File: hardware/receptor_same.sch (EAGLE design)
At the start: 62 parts, among them J1 ICSP, J2 SERIAL, J3 GPIO, J4 AUX-POWER, Q1 MMBT3904LT1G, U1 ATMEGA328P_TQFP, U2 SI4707, U3 TPA6111A2DR, U4 MCP16301/H, U5 TLV70233DBVR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

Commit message: fix mpn conector 3 pines
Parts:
- J4: MPN (none) -> P125-1103A1BS116A1
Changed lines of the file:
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@@
 <part name="GND19" library="supply1" library_urn="urn:adsk.eagle:library:371" deviceset="GND" device=""/>
 <part name="R16" library="OPL_Resistor" library_urn="urn:adsk.eagle:library:8004883" deviceset="SMD-RES-1.5K-5%-1/10W(0603)" device="" package3d_urn="urn:adsk.eagle:package:8004941/1" value="1.5K"/>
-<part name="J4" library="OPL_Connector" library_urn="urn:adsk.eagle:library:8004395" deviceset="DIP-BLACK-MALE-HEADER-VERT(3P-2.54)" device="" package3d_urn="urn:adsk.eagle:package:8004514/1" value="AUX-POWER"/>
+<part name="J4" library="OPL_Connector" library_urn="urn:adsk.eagle:library:8004395" deviceset="DIP-BLACK-MALE-HEADER-VERT(3P-2.54)" device="" package3d_urn="urn:adsk.eagle:package:8004514/1" value="AUX-POWER">
+<attribute name="MPN" value="P125-1103A1BS116A1"/>
+</part>
 <part name="P+17" library="supply1" library_urn="urn:adsk.eagle:library:371" deviceset="+3V3" device=""/>
 <part name="GND20" library="supply1" library_urn="urn:adsk.eagle:library:371" deviceset="GND" device=""/>
@@
 <attribute name="VALUE" x="96.52" y="16.51" size="1.27" layer="96" ratio="10"/>
 <attribute name="NAME" x="96.52" y="30.48" size="1.27" layer="95" ratio="10"/>
+<attribute name="MPN" x="99.06" y="24.13" size="1.778" layer="96" display="off"/>
 </instance>
 <instance part="P+17" gate="G$1" x="88.9" y="34.29" smashed="yes">

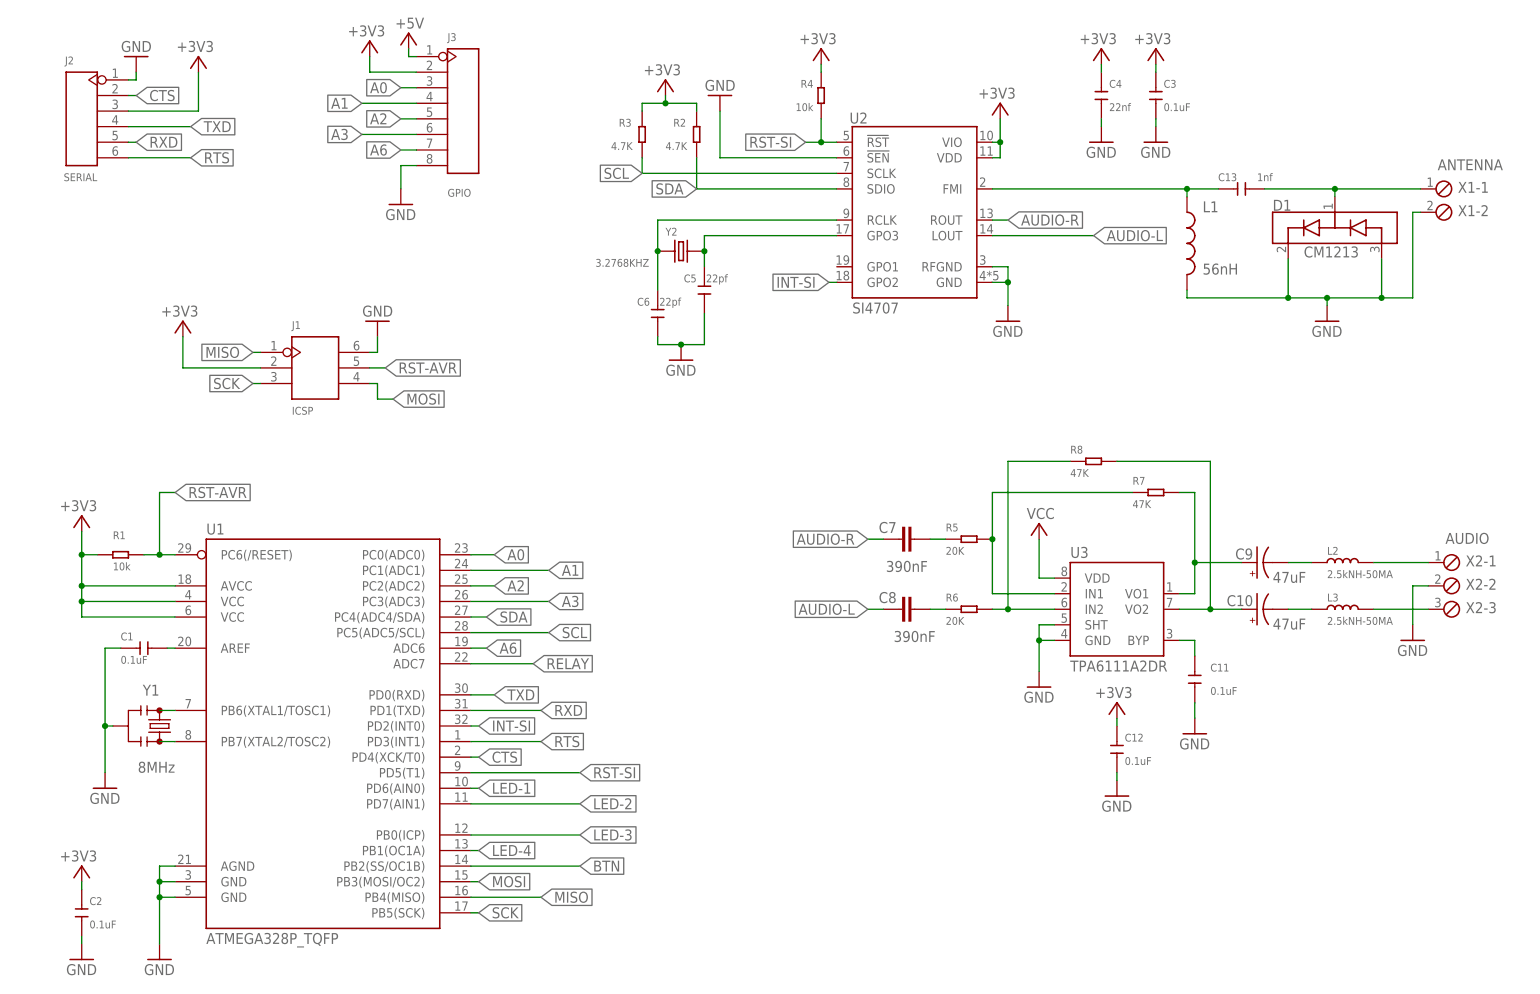
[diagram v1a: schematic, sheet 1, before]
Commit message: ajustes bom y posicion en hoja
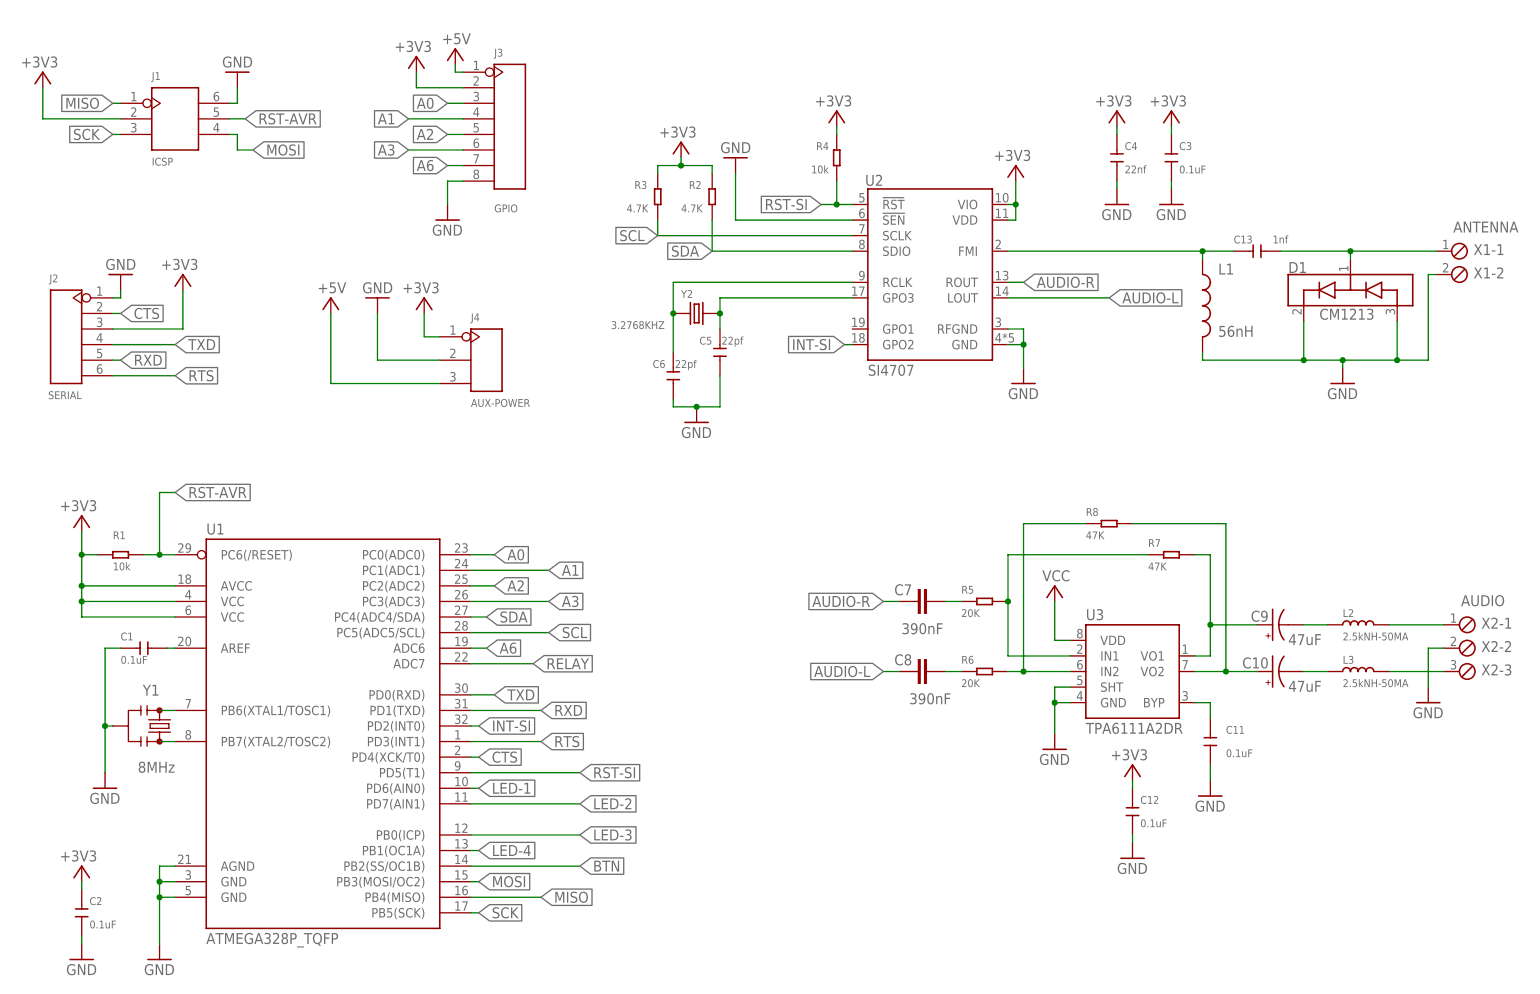
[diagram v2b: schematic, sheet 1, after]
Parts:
- C11, C12, C3: SPICEPREFIX C -> (none)
- D2: value LED-1 -> GREEN
- D3: value LED-2 -> GREEN
- K1: value (none) -> HLS8L-DC5V
- R15: value 10K -> 10k
- R4: SPICEPREFIX R -> (none)
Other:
- moved on the sheet: C10, C11, C12, C13, C3, C4, C5, C6, C7, C8, C9, D1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

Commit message: ajustamos values a mayusculas
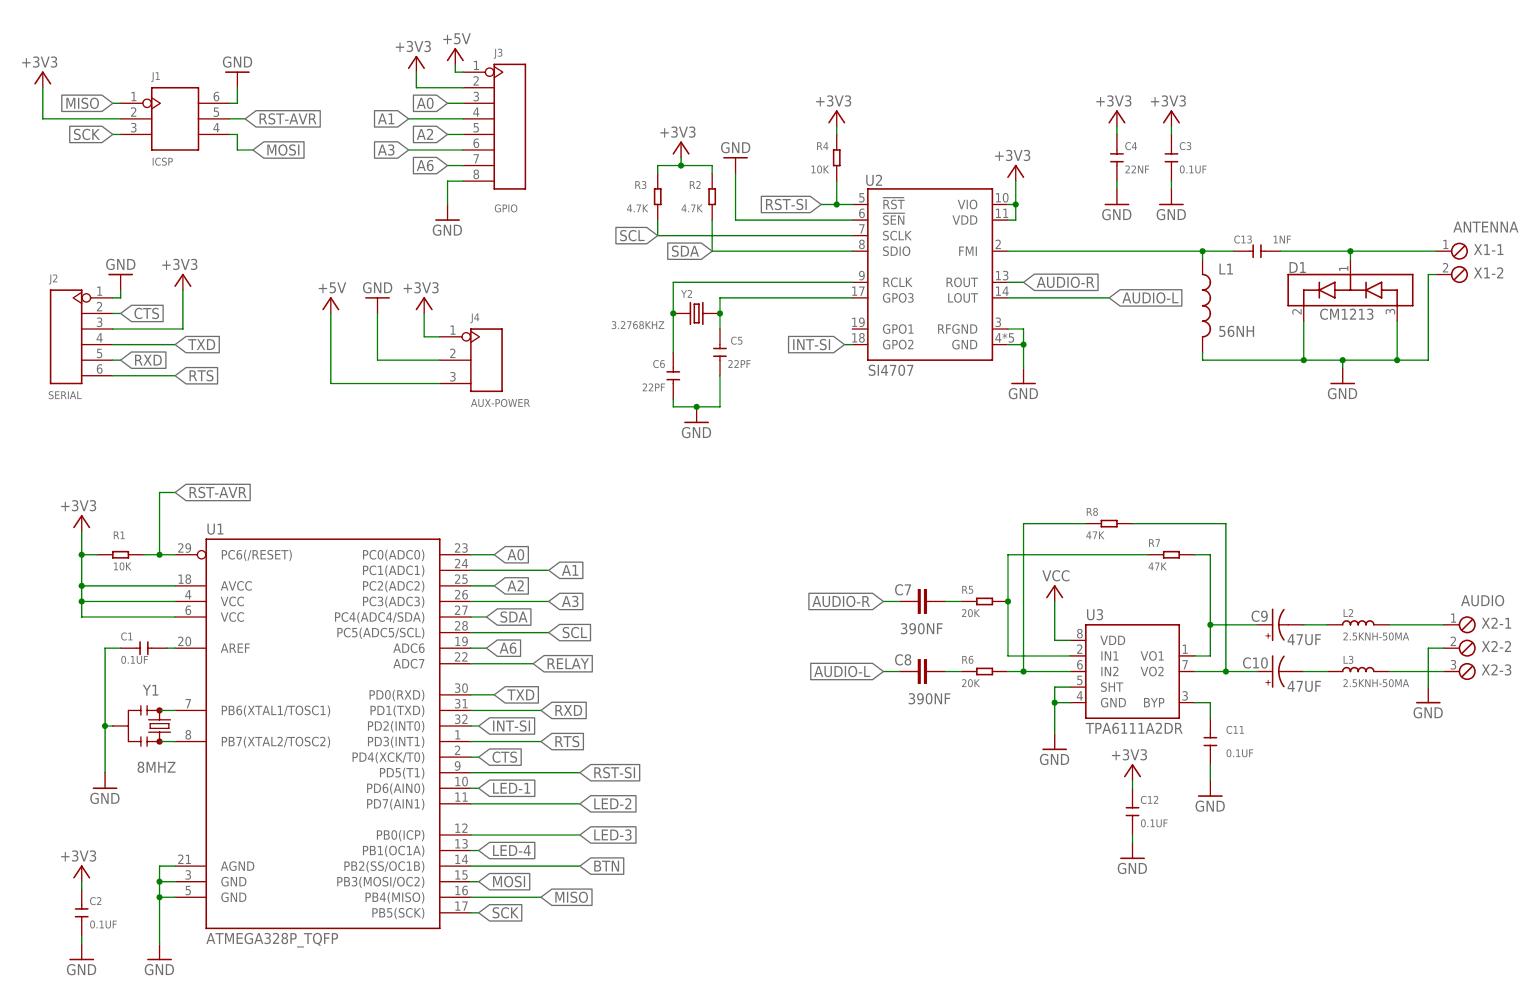
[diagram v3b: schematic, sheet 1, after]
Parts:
- C1, C11, C12, C18, C2, C3: value 0.1uF -> 0.1UF
- C10, C9: value 47uF -> 47UF
- C13: value 1nf -> 1NF
- C15: value 100nf-50V -> 100NF-50V
- C4: value 22nf -> 22NF
- C5, C6: value 22pf -> 22PF
- C7, C8: value 390nF -> 390NF
- L1: value 56nH -> 56NH
- L2, L3: value 2.5kNH-50MA -> 2.5KNH-50MA
- R1, R11, R15, R4: value 10k -> 10K
- Y1: value 8MHz -> 8MHZ

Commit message: ajutes values caps
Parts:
- C15: value 100NF-50V -> 0.1UF
- C16, C17: value 10UF-6.3V -> 10UF
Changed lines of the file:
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@@
 <setting verticaltext="up"/>
 </settings>
-<grid distance="0.05" unitdist="inch" unit="inch" style="dots" multiple="1" display="yes" altdistance="0.01" altunitdist="inch" altunit="inch"/>
+<grid distance="0.1" unitdist="inch" unit="inch" style="lines" multiple="1" display="no" altdistance="0.01" altunitdist="inch" altunit="inch"/>
 <layers>
 <layer number="1" name="Top" color="4" fill="1" visible="no" active="no"/>
@@
 <attribute name="MPN" value="CL31A106KBHNNNE"/>
 </part>
-<part name="C15" library="OPL_Capacitor" library_urn="urn:adsk.eagle:library:8004261" deviceset="CERAMIC-100NF-50V-10%-X7R(0603)" device="" package3d_urn="urn:adsk.eagle:package:8004287/1" value="100NF-50V"/>
+<part name="C15" library="OPL_Capacitor" library_urn="urn:adsk.eagle:library:8004261" deviceset="CERAMIC-100NF-50V-10%-X7R(0603)" device="" package3d_urn="urn:adsk.eagle:package:8004287/1" value="0.1UF"/>
 <part name="GND16" library="supply1" library_urn="urn:adsk.eagle:library:371" deviceset="GND" device=""/>
 <part name="D5" library="OPL_Discrete_Semiconductor" library_urn="urn:adsk.eagle:library:8004488" deviceset="SMD-DIODE-SCHOTTKY-40V-1A(DO-214AC)" device="" package3d_urn="urn:adsk.eagle:package:8004547/1" value="40V-1A"/>
@@
 <attribute name="MPN" value="WR06X5232FTL"/>
 </part>
-<part name="C16" library="OPL_Capacitor" library_urn="urn:adsk.eagle:library:8004261" deviceset="CERAMIC-10UF-6.3V-20%-X5R(0603)" device="" package3d_urn="urn:adsk.eagle:package:8004287/1" value="10UF-6.3V"/>
-<part name="C17" library="OPL_Capacitor" library_urn="urn:adsk.eagle:library:8004261" deviceset="CERAMIC-10UF-6.3V-20%-X5R(0603)" device="" package3d_urn="urn:adsk.eagle:package:8004287/1" value="10UF-6.3V"/>
+<part name="C16" library="OPL_Capacitor" library_urn="urn:adsk.eagle:library:8004261" deviceset="CERAMIC-10UF-6.3V-20%-X5R(0603)" device="" package3d_urn="urn:adsk.eagle:package:8004287/1" value="10UF"/>
+<part name="C17" library="OPL_Capacitor" library_urn="urn:adsk.eagle:library:8004261" deviceset="CERAMIC-10UF-6.3V-20%-X5R(0603)" device="" package3d_urn="urn:adsk.eagle:package:8004287/1" value="10UF"/>
 <part name="X5" library="con-phoenix-254" library_urn="urn:adsk.eagle:library:172" deviceset="MPT2" device="" package3d_urn="urn:adsk.eagle:package:9320/1" value="POWER">
 <attribute name="MPN" value="1725656"/>
